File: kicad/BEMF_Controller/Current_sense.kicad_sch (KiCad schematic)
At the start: 21 parts, among them U13 INA181, U14 INA181, U15 INA181, U2 INA181

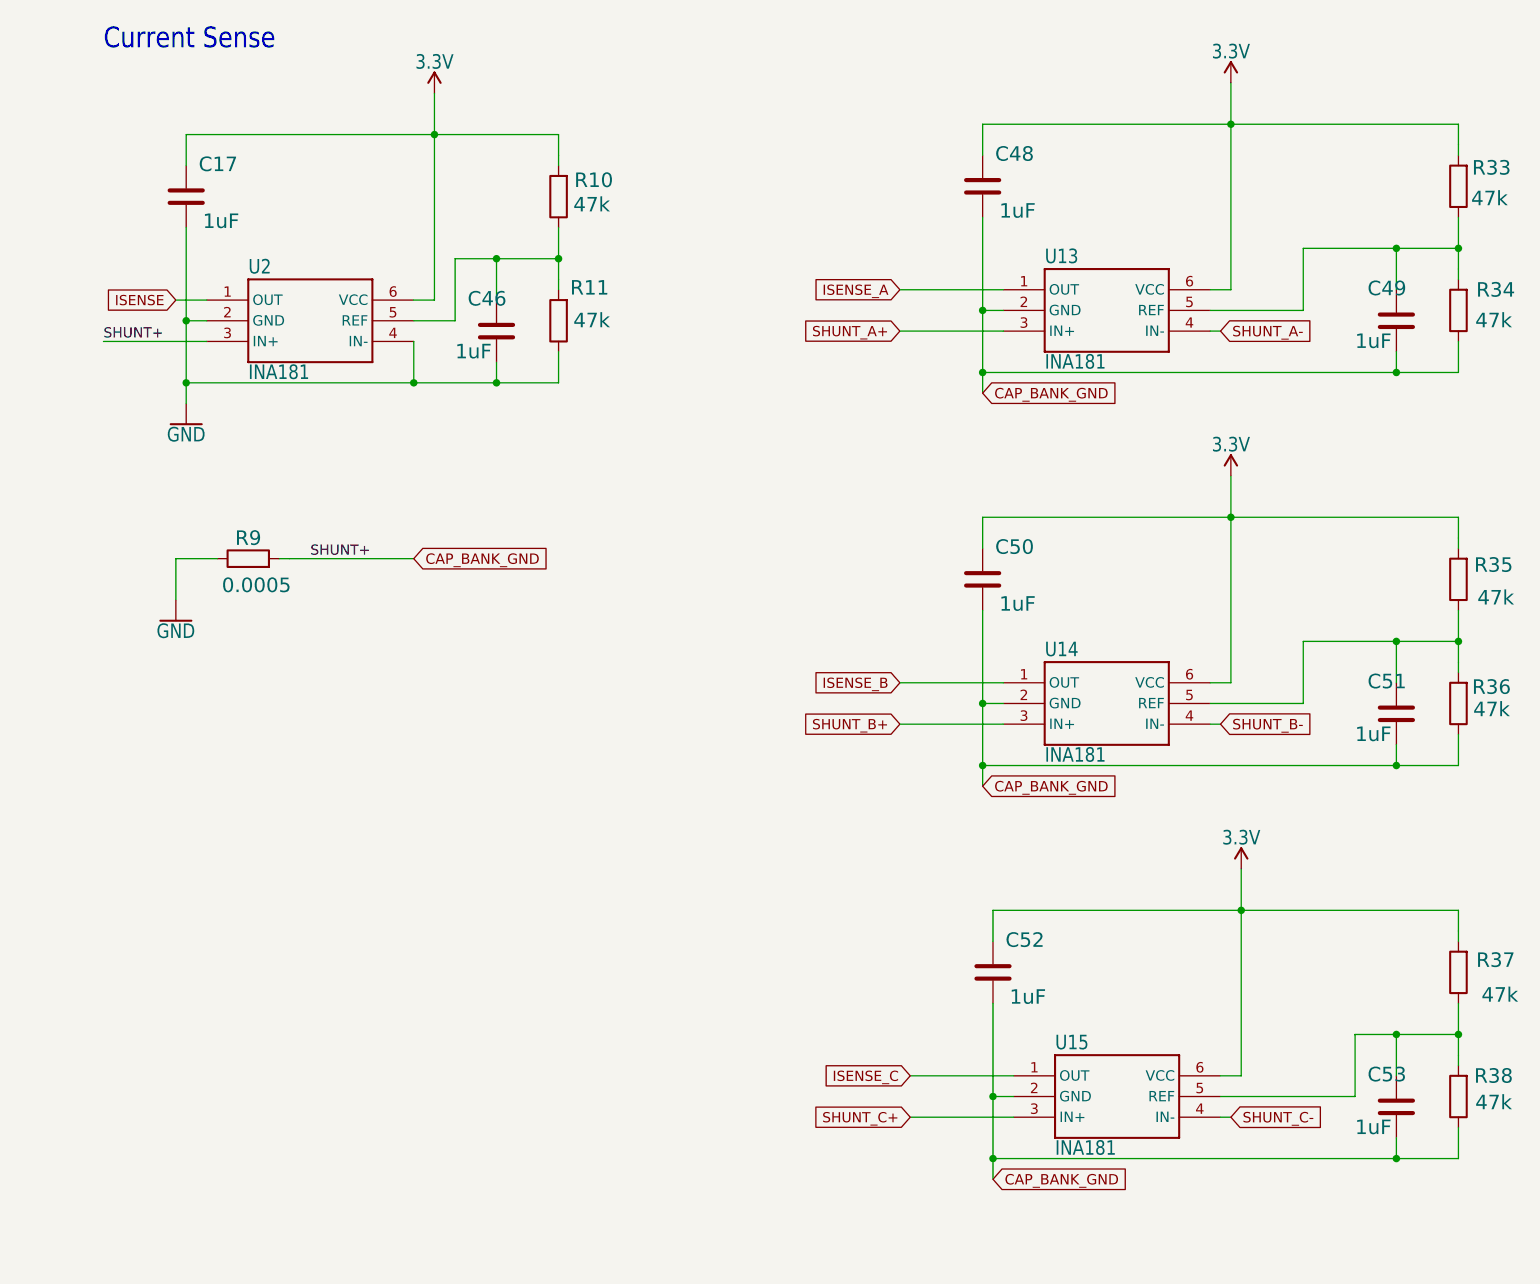
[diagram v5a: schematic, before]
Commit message: Change of plans. Make simple controller for MEG only
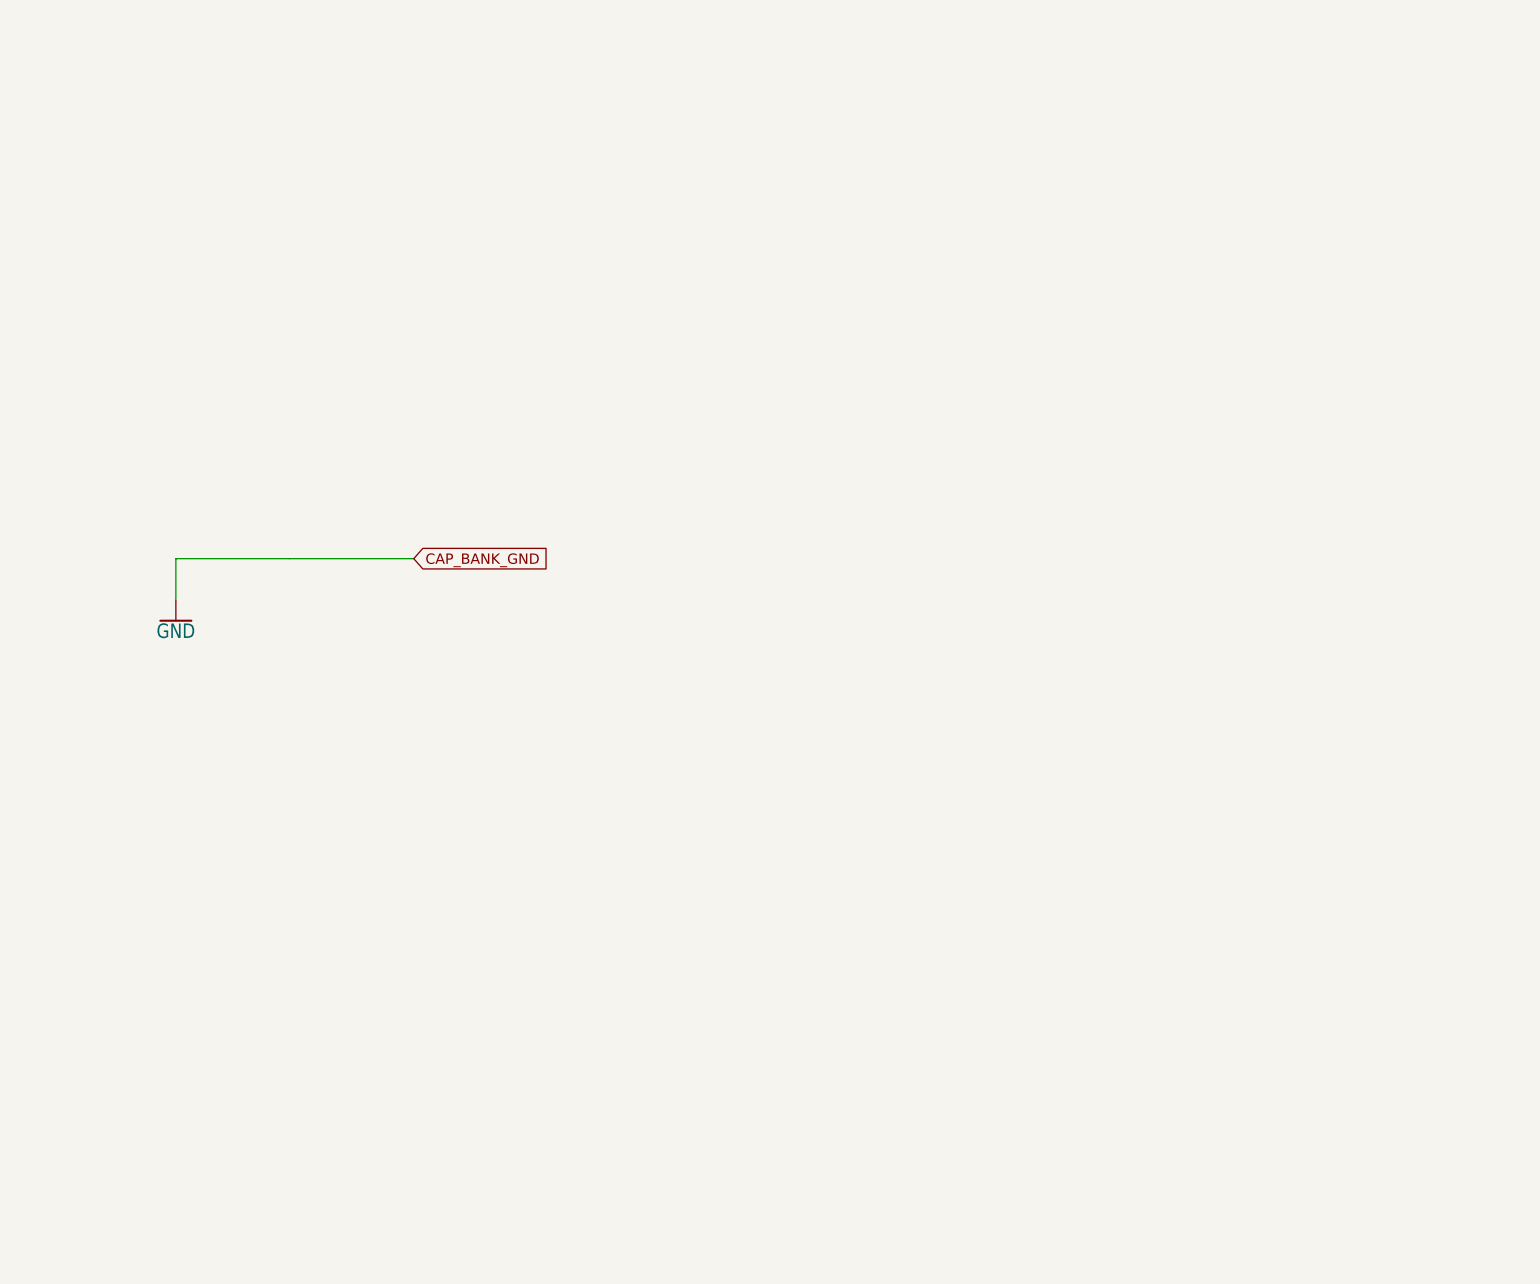
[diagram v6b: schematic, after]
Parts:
- removed C17, C46, C48, C49, C50, C51, C52, C53: 1uF, Capacitor_SMD:C_1812_4532Metric, symbol Component_Library:CHV1812N250105MXT
- removed R10, R11, R33, R34, R35, R36, R37, R38: 47k, Resistor_SMD:R_1206_3216Metric, symbol Component_Library:R47k
- removed R9: 0.0005, Resistor_SMD:R_2512_6332Metric_Pad1.40x3.35mm_HandSolder, symbol Component_Library:R0005
- removed U13, U14, U15, U2: INA181, main:SOT23-6, symbol main-eagle-import:INA181
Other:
- note removed: "Current Sense"
